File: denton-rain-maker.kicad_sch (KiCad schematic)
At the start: 63 parts, among them J1 Conn_01x06, J3 SEED C3, Q4 BT136S-800E, Q5 BT136S-800E, Q6 BT136S-800E, Q7 BT136S-800E, U4 MOC3063M, U5 LMR38010FSDDAR, U6 MOC3063M, U7 MOC3063M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

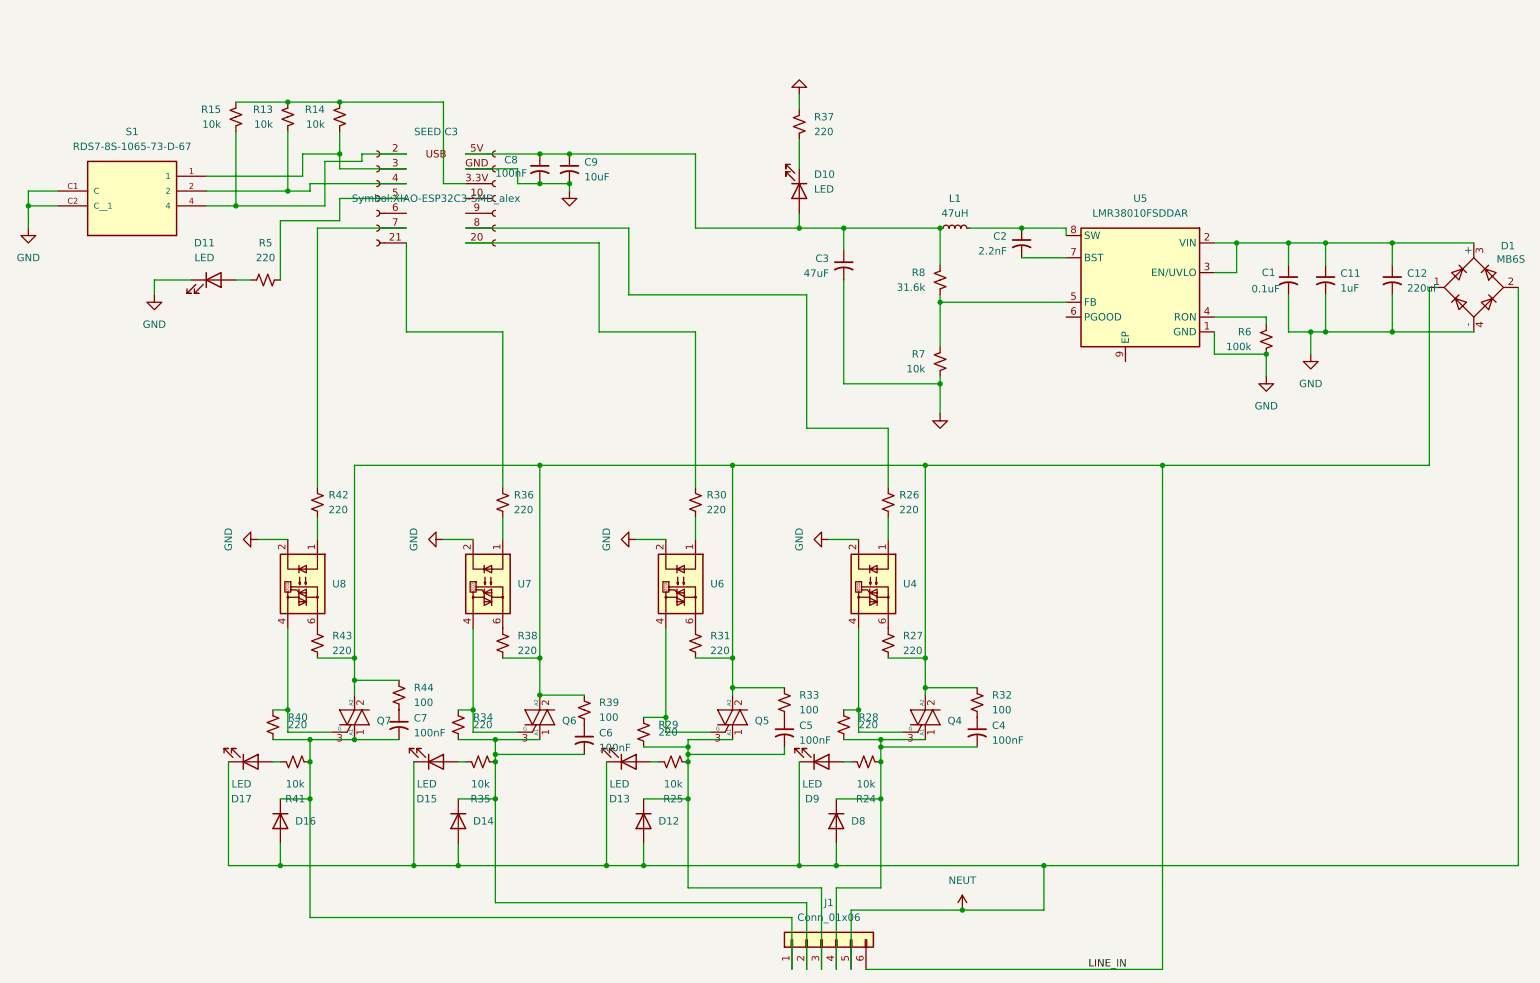
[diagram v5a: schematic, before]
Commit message: added LDO,MOV
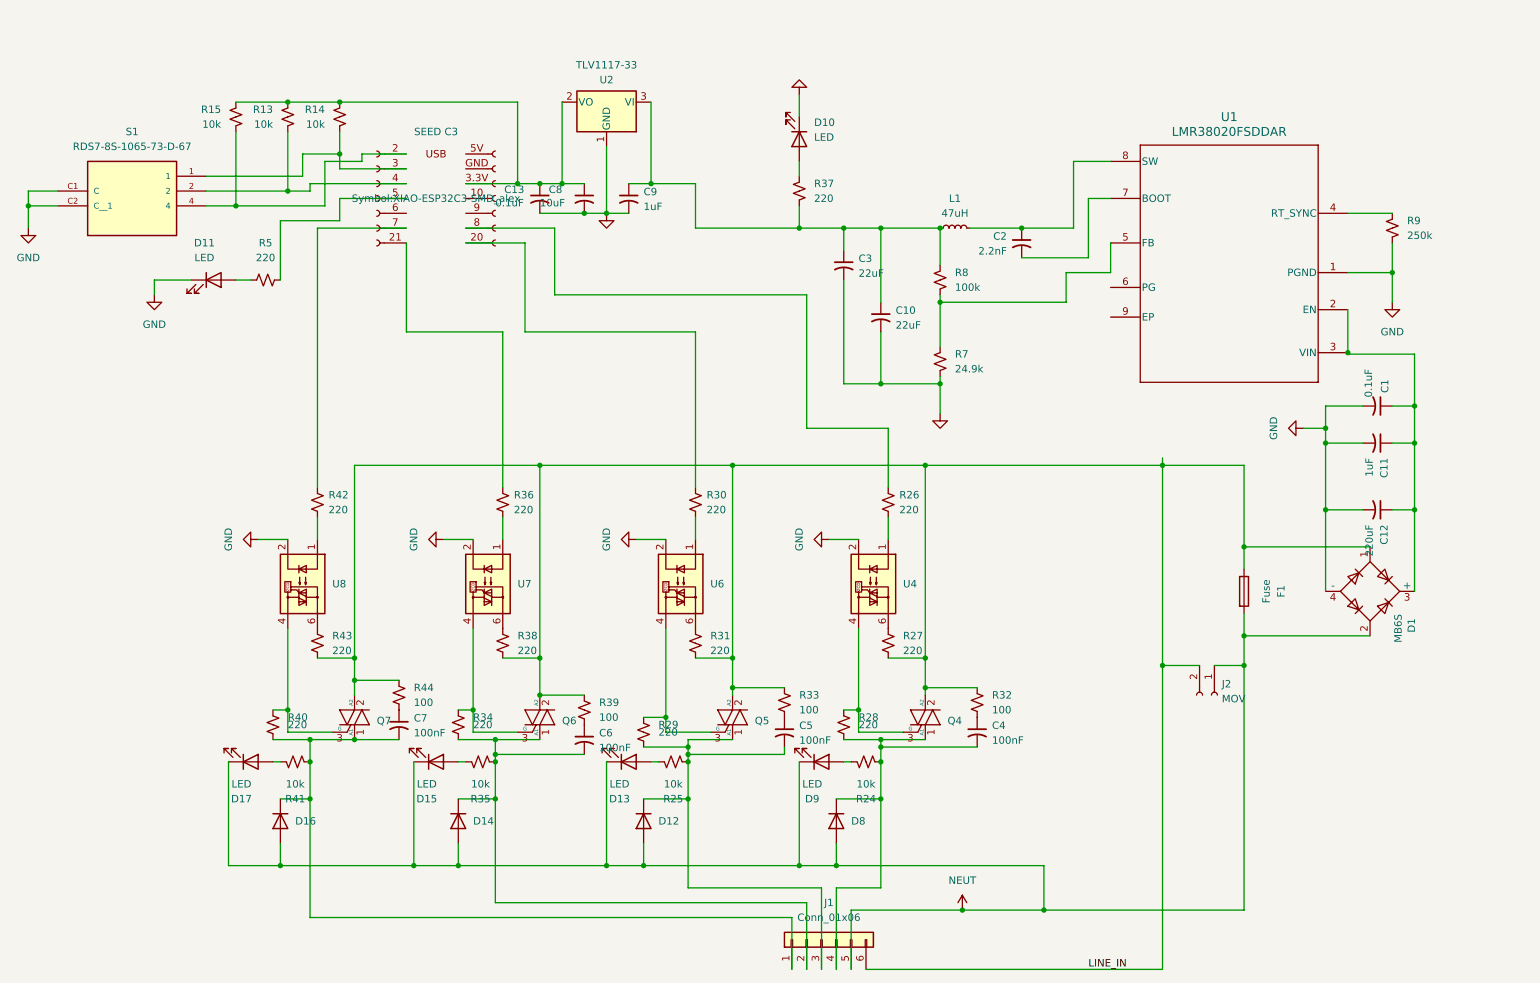
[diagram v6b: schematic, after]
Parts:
- removed R6: 100k, Resistor_SMD:R_1206_3216Metric_Pad1.30x1.75mm_HandSolder, symbol Device:R_Small_US
- removed U5: LMR38010FSDDAR, Package_SO:Texas_R-PDSO-G8_EP2.95x4.9mm_Mask2.4x3.1mm, symbol Regulator_Switching:LM5164DDA
- added C10: 22uF, Capacitor_SMD:C_1206_3216Metric_Pad1.33x1.80mm_HandSolder, symbol Device:C_Small_US
- added C13: 0.1uF, Capacitor_SMD:C_1206_3216Metric_Pad1.33x1.80mm_HandSolder, symbol Device:C_Small_US
- added F1: Fuse, Fuse:Fuseholder_Blade_Mini_Keystone_3568, symbol Device:Fuse
- added J2: MOV, Capacitor_THT:C_Disc_D7.5mm_W5.0mm_P7.50mm, symbol Connector:Conn_01x02_Socket
- added R9: 250k, Resistor_SMD:R_1206_3216Metric_Pad1.30x1.75mm_HandSolder, symbol Device:R_Small_US
- added U1: LMR38020FSDDAR, footprints:DDA0008E-IPC_C, symbol 2026-06-20_16-52-41:LMR38020FSDDAR
- added U2: TLV1117-33, Package_TO_SOT_SMD:SOT-223-3_TabPin2, symbol Regulator_Linear:TLV1117-33
- C3: value 47uF -> 22uF; footprint Capacitor_THT:CP_Radial_D6.3mm_P2.50mm -> Capacitor_SMD:C_1206_3216Metric_Pad1.33x1.80mm_HandSolder
- C8: value 100nF -> 10uF
- C9: value 10uF -> 1uF
- R7: value 10k -> 24.9k
- R8: value 31.6k -> 100k
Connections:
- net GND: now also D10.1 (K), C10.2, C13.2, R9.2, U1.1 (PGND), U2.1 (GND); no longer J3.GND (Pin_2), R37.1
- net LINE_IN: now also F1.1, J2.2 (Pin_2)
- net NEUT: now also F1.2, J2.1 (Pin_1)
- net at J3.3.3V (Pin_3), R13.1, R14.1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: now also C8.1, C13.1, U2.2 (VO)
- net at R37.2: now also C3.1, C9.1, L1.2, R8.1, C10.1, U2.3 (VI); no longer D10.1 (K)
- net at C1.1, C11.1, C12.1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: now also U1.2 (EN), U1.3 (VIN)
- net at R7.1, R8.2: now also U1.5 (FB)
- net at C2.1, L1.1: now also U1.8 (SW)
- net at C2.2: now also U1.7 (BOOT)
- new net: D10.2 (A), R37.1
- new net: R9.1, U1.4 (RT_SYNC)
- now unconnected: J3.5V (Pin_1)
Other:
- moved on the sheet: C1, C11, C12, C8, C9, D1, D10, R37

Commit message: new pwr supply
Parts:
- removed C10, C3: 22uF, Capacitor_SMD:C_1206_3216Metric_Pad1.33x1.80mm_HandSolder, symbol Device:C_Small_US
- removed C2: 2.2nF, Capacitor_SMD:C_1206_3216Metric_Pad1.33x1.80mm_HandSolder, symbol Device:C_Small_US
- removed L1: 47uH, Inductor_SMD:L_Bourns_SRN6045TA, symbol Device:L_Small
- removed R7: 24.9k, Resistor_SMD:R_1206_3216Metric_Pad1.30x1.75mm_HandSolder, symbol Device:R_Small_US
- removed R8: 100k, Resistor_SMD:R_1206_3216Metric_Pad1.30x1.75mm_HandSolder, symbol Device:R_Small_US
- removed R9: 250k, Resistor_SMD:R_1206_3216Metric_Pad1.30x1.75mm_HandSolder, symbol Device:R_Small_US
- removed U1: LMR38020FSDDAR, footprints:DDA0008E-IPC_C, symbol 2026-06-20_16-52-41:LMR38020FSDDAR
- added C14: 220uF, Capacitor_THT:CP_Radial_D10.0mm_P5.00mm, symbol Device:C_Small_US
- added D2: D_Schottky_Small, Diode_SMD:D_MicroSMP_LargeCathode, symbol Device:D_Schottky_Small
- added L2: NRS6028T330MMGJ, inductor:IND_TAIYO_NRS6028_TAY, symbol 2026-06-23_19-00-12:NRS6028T330MMGJ
- added U1: LM2596S-5, Package_TO_SOT_SMD:TO-263-5_TabPin3, symbol Regulator_Switching:LM2596S-5
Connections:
- net GND: now also C14.2, D2.2 (A), U1.3 (GND), U1.5 (~{ON}/OFF)
- net at C9.1, R37.2, U2.3 (VI): now also C14.1, L2.2, U1.4 (FB)
- net at C1.1, C11.1, C12.1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: now also U1.1 (VIN)
- new net: D2.1 (K), L2.1, U1.2 (OUT)
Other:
- moved on the sheet: C1, C11, C12
